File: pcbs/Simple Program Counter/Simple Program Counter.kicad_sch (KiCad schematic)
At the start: 0 parts

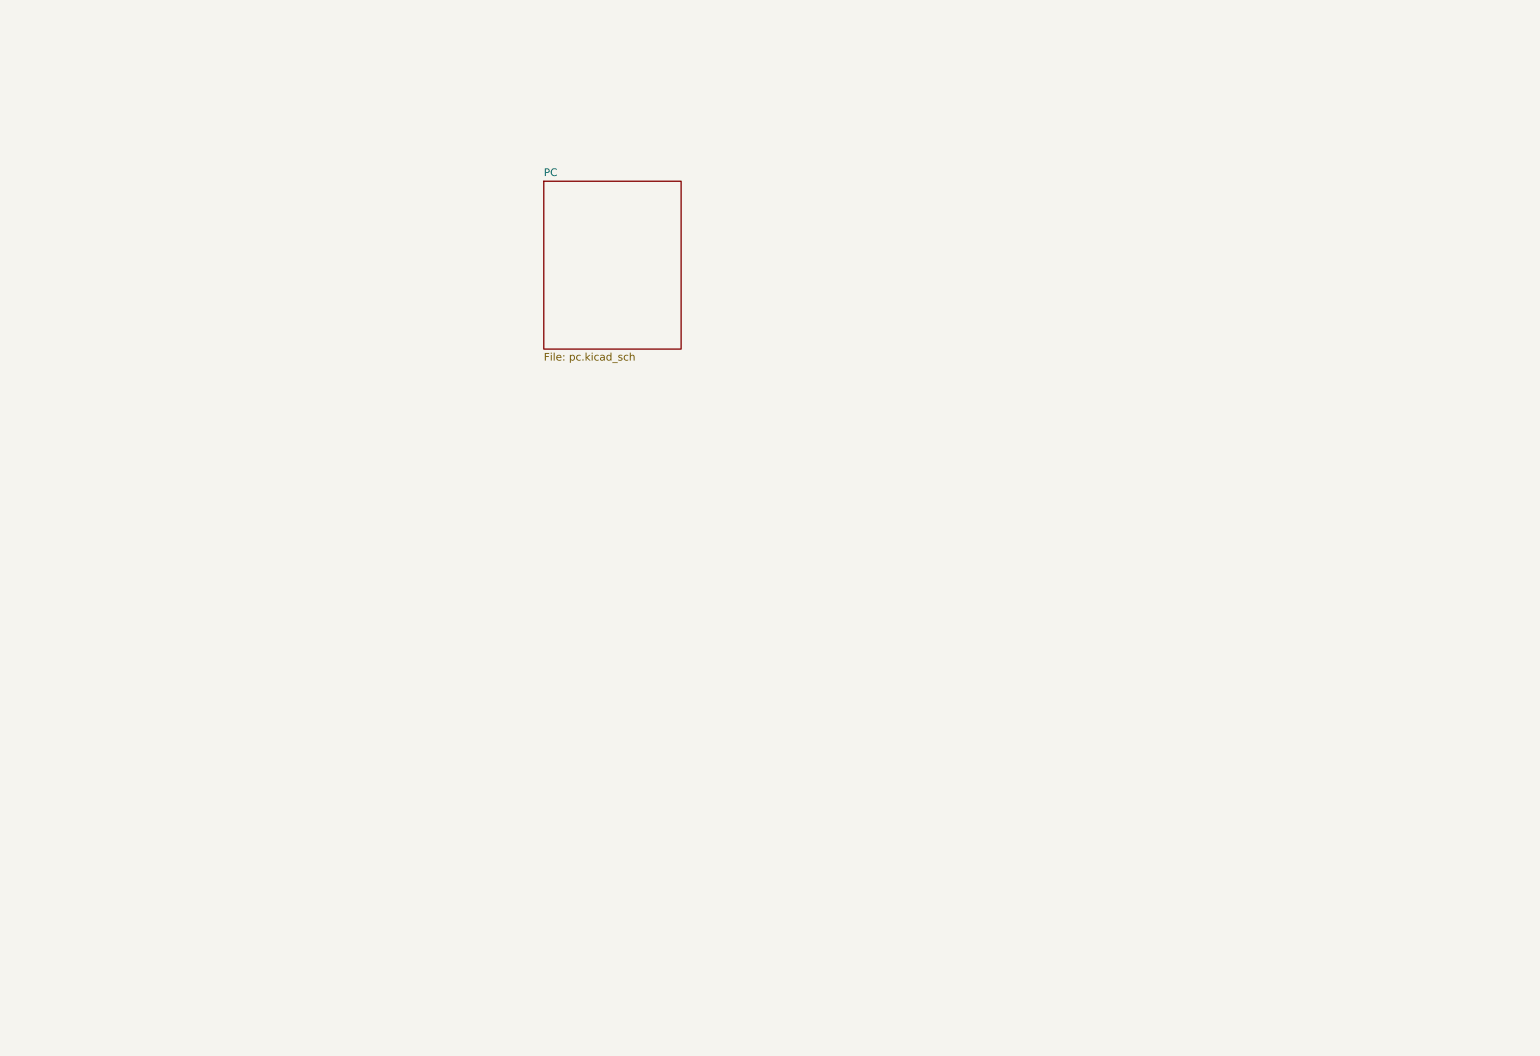
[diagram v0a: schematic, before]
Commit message: Adding indicator LEDs
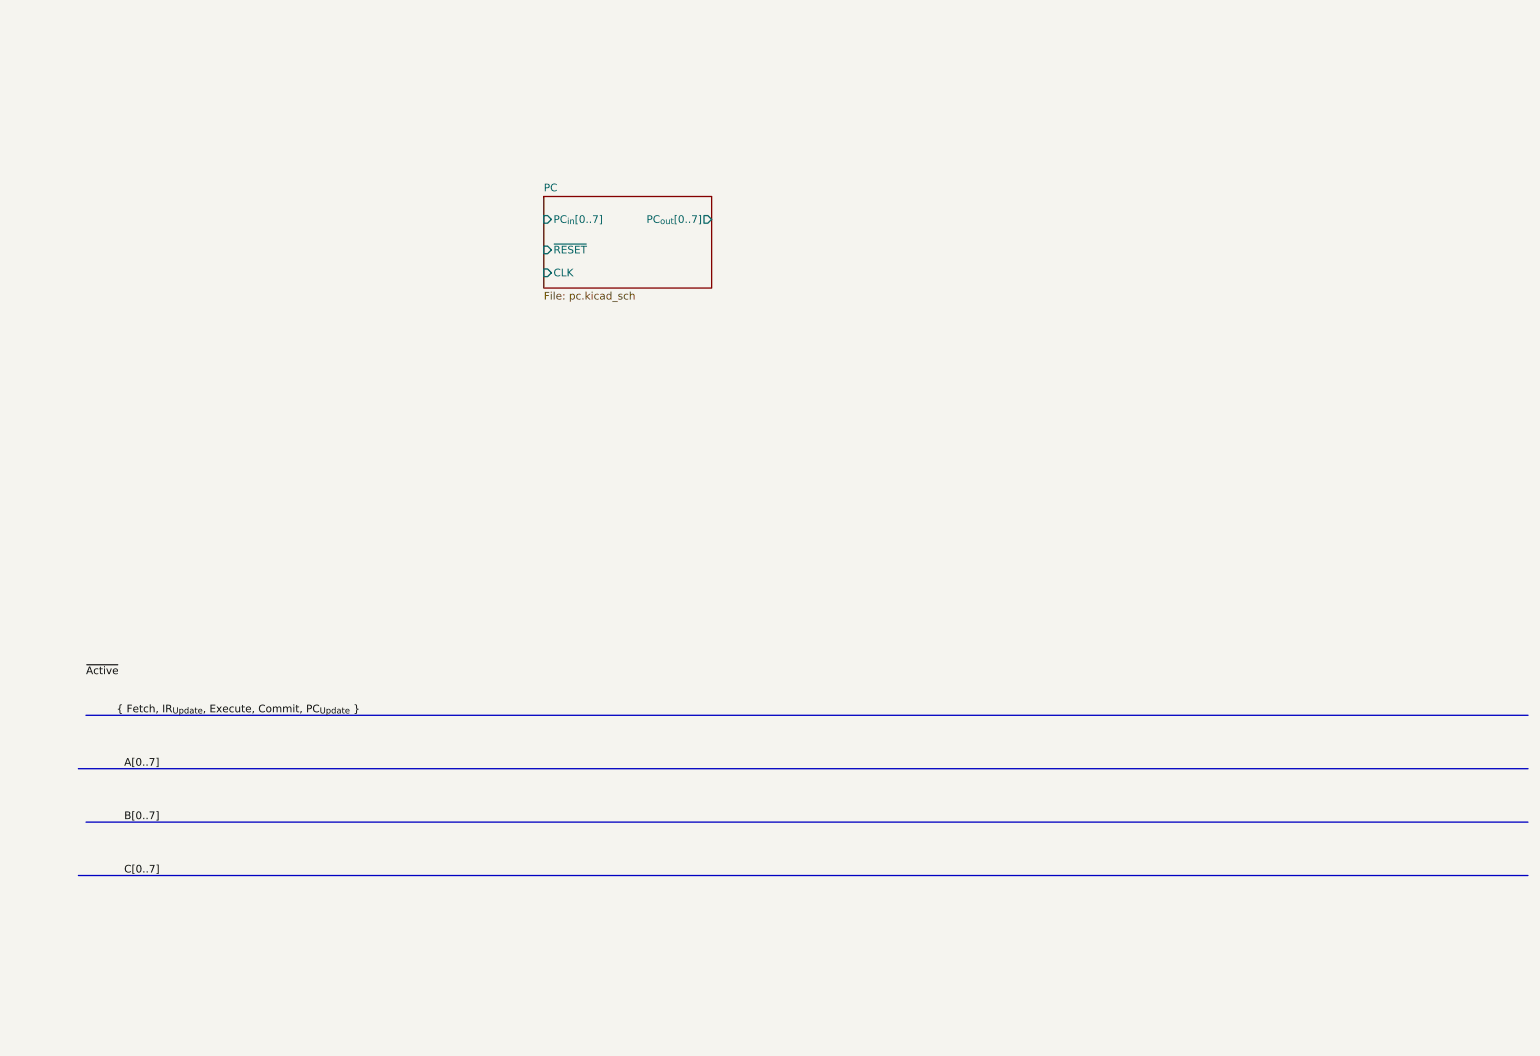
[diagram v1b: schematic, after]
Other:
- sheet PC ports: added CLK, PC_{in}[0..7], PC_{out}[0..7], ~{RESET}; removed none
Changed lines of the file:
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@@
 (kicad_sch (version 20230121) (generator eeschema)
   (paper "A4")
-  (sheet (at 101.6 45.72) (size 22.86 27.94) (fields_autoplaced)
+  (bus (pts (xy 25.4 152.4) (xy 265.43 152.4))
+    (stroke (width 0) (type default))
+  )
+  (bus (pts (xy 24.13 143.51) (xy 265.43 143.51))
+    (stroke (width 0) (type default))
+  )
+  (bus (pts (xy 24.13 161.29) (xy 265.43 161.29))
+    (stroke (width 0) (type default))
+  )
+  (bus (pts (xy 25.4 134.62) (xy 265.43 134.62))
+    (stroke (width 0) (type default))
+  )
+  (label "{ Fetch, IR_{Update}, Execute, Commit, PC_{Update} }"
+    (at 30.48 134.62 0) (fields_autoplaced)
+    (effects (font (size 1.27 1.27)) (justify left bottom))
+  )
+  (label "~{Active}" (at 25.4 128.27 0) (fields_autoplaced)
+    (effects (font (size 1.27 1.27)) (justify left bottom))
+  )
+  (label "A[0..7]" (at 31.75 143.51 0) (fields_autoplaced)
+    (effects (font (size 1.27 1.27)) (justify left bottom))
+  )
+  (label "C[0..7]" (at 31.75 161.29 0) (fields_autoplaced)
+    (effects (font (size 1.27 1.27)) (justify left bottom))
+  )
+  (label "B[0..7]" (at 31.75 152.4 0) (fields_autoplaced)
+    (effects (font (size 1.27 1.27)) (justify left bottom))
+  )
+  (sheet (at 101.6 48.26) (size 27.94 15.24) (fields_autoplaced)
     (stroke (width 0.1524) (type solid))
     (fill (color 0 0 0 0.0000))
-    (property "Sheetname" "PC" (at 101.6 45.0084 0)
+    (property "Sheetname" "PC" (at 101.6 47.5484 0)
       (effects (font (size 1.27 1.27)) (justify left bottom))
     )
-    (property "Sheetfile" "pc.kicad_sch" (at 101.6 74.2446 0)
+    (property "Sheetfile" "pc.kicad_sch" (at 101.6 64.0846 0)
       (effects (font (size 1.27 1.27)) (justify left top))
     )
+    (pin "PC_{in}[0..7]" input (at 101.6 52.07 180)
+      (effects (font (size 1.27 1.27)) (justify left))
+    )
+    (pin "~{RESET}" input (at 101.6 57.15 180)
+      (effects (font (size 1.27 1.27)) (justify left))
+    )
+    (pin "CLK" input (at 101.6 60.96 180)
+      (effects (font (size 1.27 1.27)) (justify left))
+    )
+    (pin "PC_{out}[0..7]" output (at 129.54 52.07 0)
+      (effects (font (size 1.27 1.27)) (justify right))
+    )
     (instances

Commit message: Thinking through some next bits
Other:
- added sheet Incrementer (incrementer.kicad_sch)
- added sheet Instructions (instructions.kicad_sch)
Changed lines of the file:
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@@
 (kicad_sch (version 20230121) (generator eeschema)
   (paper "A4")
+  (bus (pts (xy 129.54 25.4) (xy 142.24 25.4))
+    (stroke (width 0) (type default))
+  )
   (bus (pts (xy 25.4 152.4) (xy 265.43 152.4))
     (stroke (width 0) (type default))
@@
     (stroke (width 0) (type default))
   )
+  (bus (pts (xy 129.54 63.5) (xy 142.24 63.5))
+    (stroke (width 0) (type default))
+  )
   (bus (pts (xy 24.13 161.29) (xy 265.43 161.29))
     (stroke (width 0) (type default))
   )
   (bus (pts (xy 25.4 134.62) (xy 265.43 134.62))
+    (stroke (width 0) (type default))
+  )
+  (bus (pts (xy 142.24 25.4) (xy 142.24 63.5))
     (stroke (width 0) (type default))
   )
@@
     (effects (font (size 1.27 1.27)) (justify left bottom))
   )
-  (sheet (at 101.6 48.26) (size 27.94 15.24) (fields_autoplaced)
+  (sheet (at 101.6 20.32) (size 27.94 20.32) (fields_autoplaced)
     (stroke (width 0.1524) (type solid))
     (fill (color 0 0 0 0.0000))
-    (property "Sheetname" "PC" (at 101.6 47.5484 0)
+    (property "Sheetname" "Incrementer" (at 101.6 19.6084 0)
       (effects (font (size 1.27 1.27)) (justify left bottom))
     )
-    (property "Sheetfile" "pc.kicad_sch" (at 101.6 64.0846 0)
+    (property "Sheetfile" "incrementer.kicad_sch" (at 101.6 41.2246 0)
       (effects (font (size 1.27 1.27)) (justify left top))
     )
-    (pin "PC_{in}[0..7]" input (at 101.6 52.07 180)
+    (pin "~{HALT}" input (at 129.54 36.83 0)
+      (effects (font (size 1.27 1.27)) (justify right))
+    )
+    (pin "PC_{curr}[0..7]" input (at 129.54 25.4 0)
+      (effects (font (size 1.27 1.27)) (justify right))
+    )
+    (instances
+      (project "Simple Program Counter"
+        (path "/4f63efd2-c13f-4abc-af18-011a9cace63e" (page "3"))
+      )
+    )
+  )
+  (sheet (at 101.6 59.69) (size 27.94 15.24) (fields_autoplaced)
+    (stroke (width 0.1524) (type solid))
+    (fill (color 0 0 0 0.0000))
+    (property "Sheetname" "PC" (at 101.6 58.9784 0)
+      (effects (font (size 1.27 1.27)) (justify left bottom))
+    )
+    (property "Sheetfile" "pc.kicad_sch" (at 101.6 75.5146 0)
+      (effects (font (size 1.27 1.27)) (justify left top))
+    )
+    (pin "PC_{in}[0..7]" input (at 101.6 63.5 180)
       (effects (font (size 1.27 1.27)) (justify left))
     )
-    (pin "~{RESET}" input (at 101.6 57.15 180)
+    (pin "~{RESET}" input (at 101.6 68.58 180)
       (effects (font (size 1.27 1.27)) (justify left))
     )
-    (pin "CLK" input (at 101.6 60.96 180)
+    (pin "CLK" input (at 101.6 72.39 180)
       (effects (font (size 1.27 1.27)) (justify left))
     )
-    (pin "PC_{out}[0..7]" output (at 129.54 52.07 0)
+    (pin "PC_{out}[0..7]" output (at 129.54 63.5 0)
       (effects (font (size 1.27 1.27)) (justify right))
     )
@@
       )
     )
+  )
+  (sheet (at 52.07 20.32) (size 36.83 54.61) (fields_autoplaced)
+    (stroke (width 0.1524) (type solid))
+    (fill (color 0 0 0 0.0000))
+    (property "Sheetname" "Instructions" (at 52.07 19.6084 0)
+      (effects (font (size 1.27 1.27)) (justify left bottom))
+    )
+    (property "Sheetfile" "instructions.kicad_sch" (at 52.07 75.5146 0)
+      (effects (font (size 1.27 1.27)) (justify left top))
+    )
+    (instances
+      (project "Simple Program Counter"
+        (path "/4f63efd2-c13f-4abc-af18-011a9cace63e" (page "4"))
+      )
+    )

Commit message: Getting close
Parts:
- added U101: 74HC00, Package_DIP:DIP-14_W7.62mm_Socket, symbol 74xx:74HC00
- added U202: 74HC245, Package_SO:SOIC-20W_7.5x12.8mm_P1.27mm, symbol 74xx:74HC245
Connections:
- new net: U101.10, U101.6
- new net: U101.3, U101.9
- new net: U101.12, U101.13, U101.8
- new net: U101.11, U202.19 (CE)
- new net +5V: U101.14 (VCC), U202.1 (A->B), U202.20 (VCC)
- new net A0: U202.18 (B0)
- new net A1: U202.17 (B1)
- new net A2: U202.16 (B2)
- new net A3: U202.15 (B3)
- new net A4: U202.14 (B4)
- new net A5: U202.13 (B5)
- new net A6: U202.12 (B6)
- new net A7: U202.11 (B7)
- new net Fetch: U101.1, U101.2
- new net GND: U101.7 (GND), U202.10 (GND)
- new net IR_{Update}: U101.4, U101.5
- new net PC_{out}0: U202.2 (A0)
- new net PC_{out}1: U202.3 (A1)
- new net PC_{out}2: U202.4 (A2)
- new net PC_{out}3: U202.5 (A3)
- new net PC_{out}4: U202.6 (A4)
- new net PC_{out}5: U202.7 (A5)
- new net PC_{out}6: U202.8 (A6)
- new net PC_{out}7: U202.9 (A7)
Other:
- sheet Incrementer ports: added PC_{inc}[0..7]; removed none
- sheet Instructions ports: added A[0..7], B[0..7], C[0..7], Commit, Execute, I[0..3], PC_{Update}, PC_{curr}[0..7], PC_{inc}[0..7], PC_{next}[0..7], ~{Active}, ~{HALT}; removed none
